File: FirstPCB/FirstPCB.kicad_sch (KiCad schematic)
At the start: 5 parts, among them U1 STM32G0B1KETx

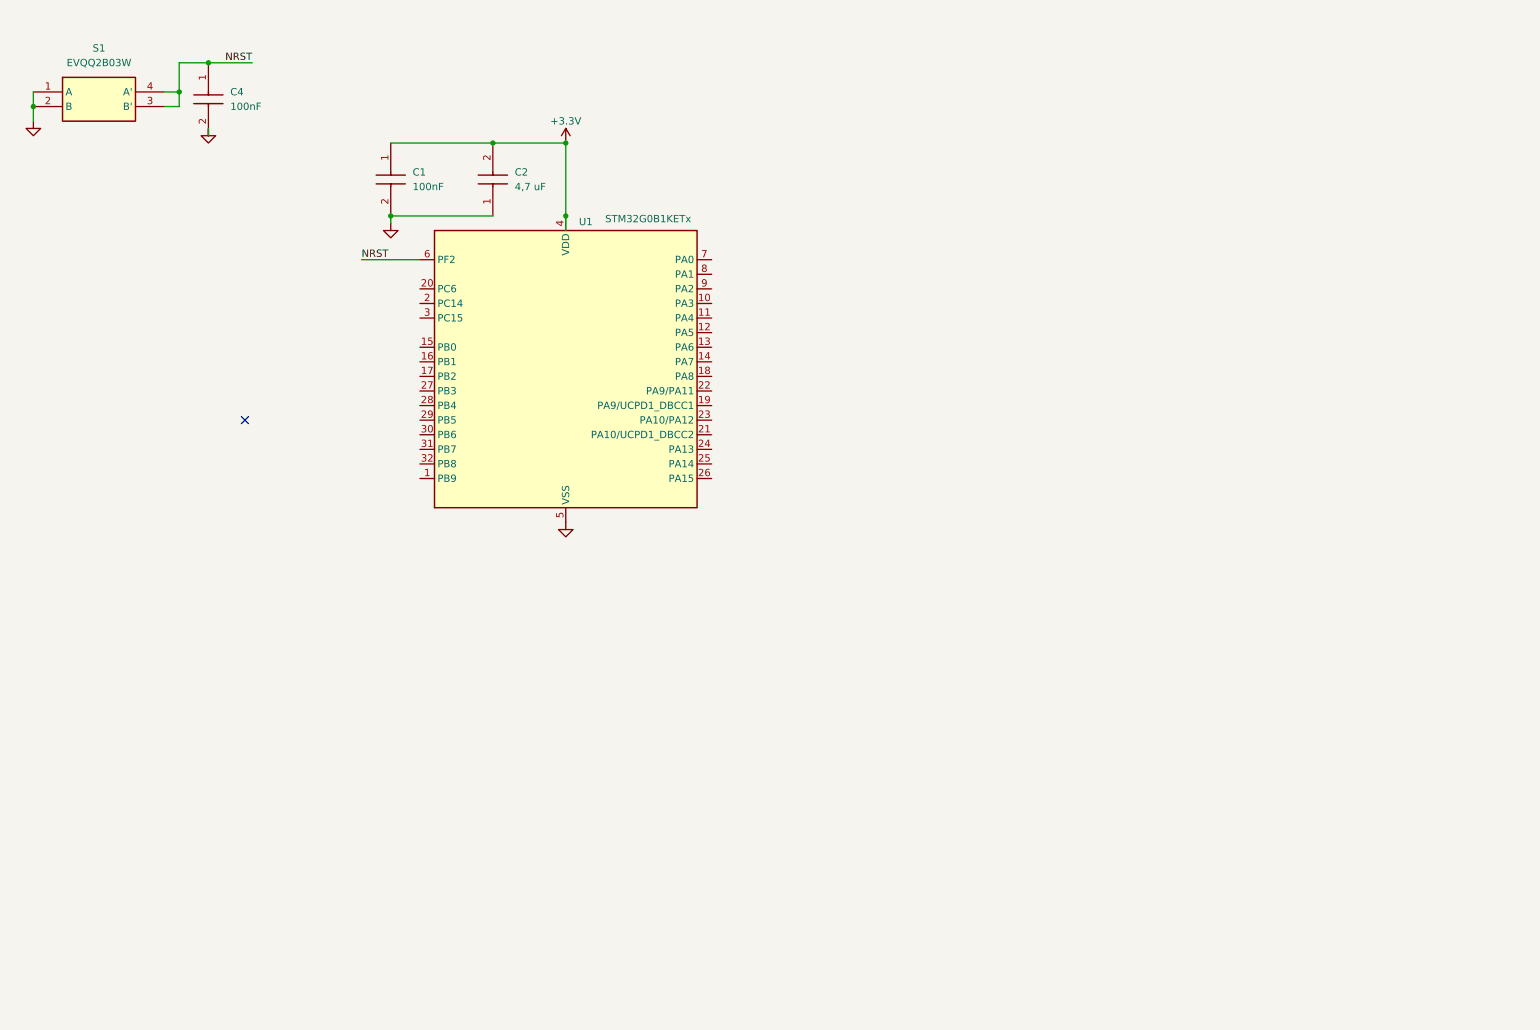
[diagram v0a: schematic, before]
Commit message: added Voltage Regulator
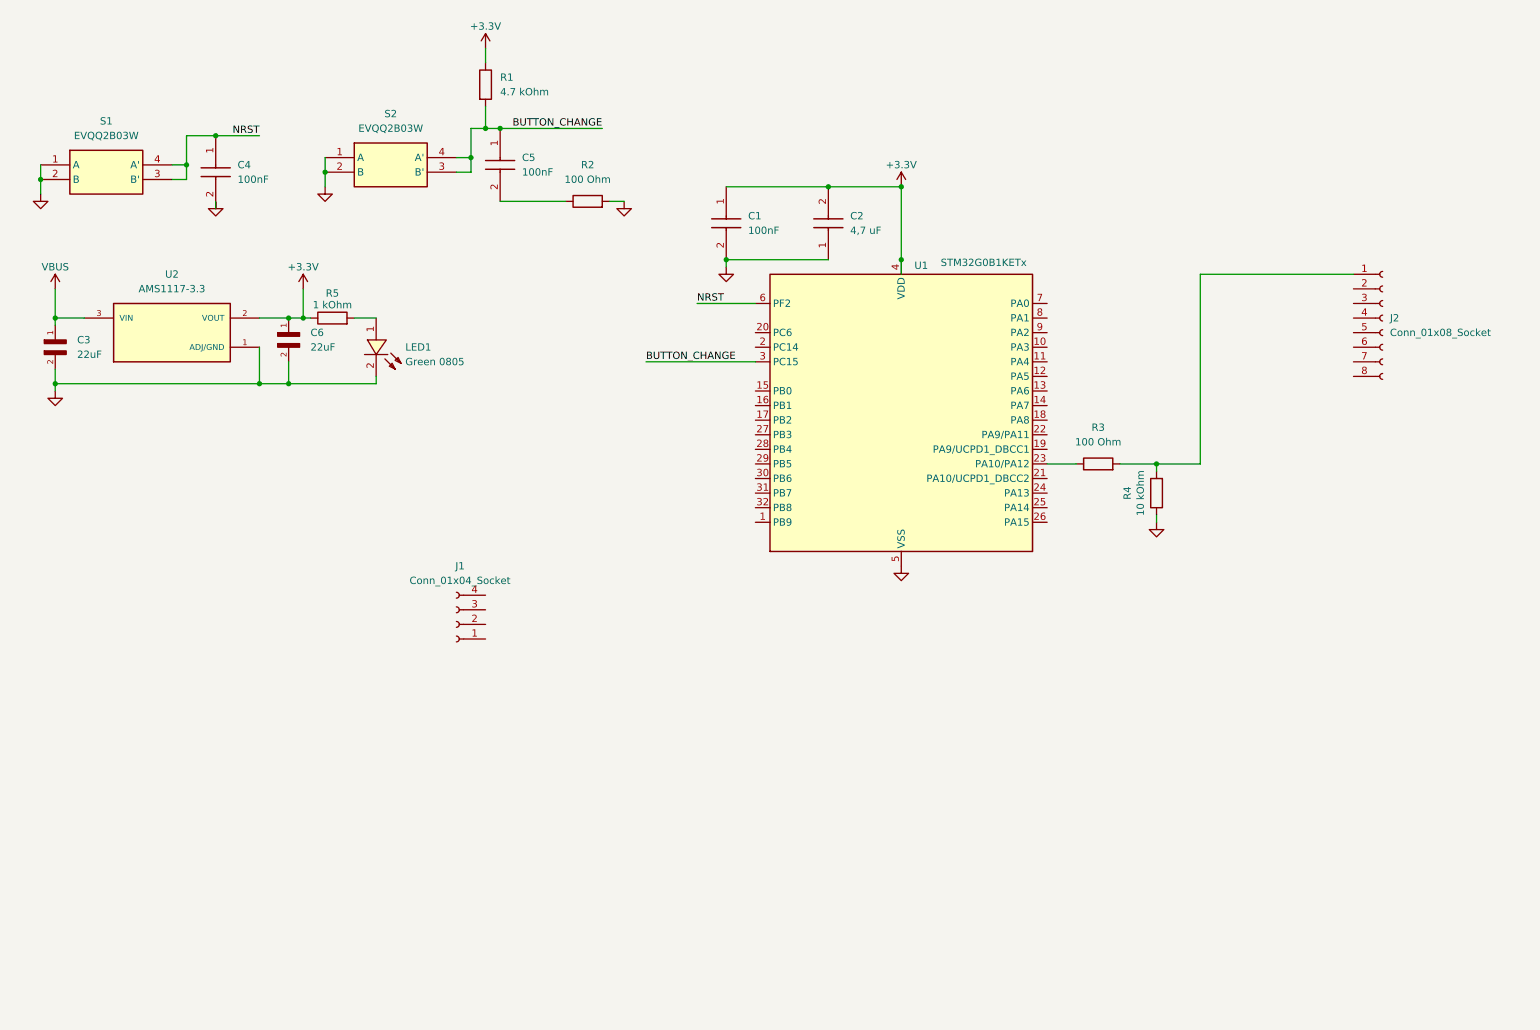
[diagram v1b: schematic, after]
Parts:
- added C3, C6: 22uF, CL21A226MQQNNNE:CAPC2012X140N, symbol CL21A226MQQNNNE:CL21A226MQQNNNE
- added C5: 100nF, SamacSys_Parts:CAPC2012X95N, symbol SamacSys_Parts:CL21B104KBCNNNC
- added J1: Conn_01x04_Socket, Connector_PinSocket_2.54mm:PinSocket_1x04_P2.54mm_Vertical, symbol Connector:Conn_01x04_Socket
- added J2: Conn_01x08_Socket, Connector_PinSocket_2.54mm:PinSocket_1x08_P2.54mm_Vertical, symbol Connector:Conn_01x08_Socket
- added LED1: Green 0805, C2292:LED0805-R-RD, symbol Yellow_green_0805:Yellowgreen0805
- added R1: 4.7 kOhm, Resistor_SMD:R_0805_2012Metric, symbol Device:R
- added R2, R3: 100 Ohm, Resistor_SMD:R_0805_2012Metric, symbol Device:R
- added R4: 10 kOhm, Resistor_SMD:R_0805_2012Metric, symbol Device:R
- added R5: 1 kOhm, Resistor_SMD:R_0805_2012Metric, symbol Device:R
- added S2: EVQQ2B03W, SamacSys_Parts:EVQQ2, symbol SamacSys_Parts:EVQQ2B03W
- added U2: AMS1117-3.3, AMS1117-3.3:SOT229P700X180-4N, symbol AMS1117-3.3:AMS1117-3.3
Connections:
- net +3.3V: now also C6.1, R1.1, R5.1, U2.2 (VOUT)
- net GND: now also C3.2, C6.2, LED1.2, R2.2, R4.1, S2.1 (A), S2.2 (B), U2.1 (ADJ/GND)
- net at U1.23 (PA10/PA12): now also R3.1
- net BUTTON_CHANGE: now reaches U1.3 (PC15)
- net BUTTON_CHANGE: now also C5.1, R1.2, S2.3 (B'), S2.4 (A')
- new net: J2.1 (Pin_1), R3.2, R4.2
- new net: C5.2, R2.1
- new net: LED1.1, R5.2
- new net VBUS: C3.1, U2.3 (VIN)
- no-connect marks 1 -> 0
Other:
- moved on the sheet: C1, C2, C4, S1, U1

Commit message: added sensor and schematic update
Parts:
- added IC1: ENS210-LQFM, SON95P200X200X80-5N, symbol SamacSys_Parts:ENS210-LQFM
- added J3, J4, J5: Conn_01x04_Socket, Connector_PinSocket_2.54mm:PinSocket_1x04_P2.54mm_Vertical, symbol Connector:Conn_01x04_Socket
- added R6, R7: 4.7 kOhm, Resistor_SMD:R_0805_2012Metric, symbol Device:R
- renumbered J2 to J1, J1 to J2
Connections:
- net +3.3V: now also J1.8 (Pin_8), IC1.1 (VDD), J3.1 (Pin_1), R6.1, R7.1
- net GND: now also J1.7 (Pin_7), IC1.4 (VSS_1), IC1.5 (VSS_2), J3.4 (Pin_4)
- net UART_RX: now reaches U1.10 (PA3)
- net UART_RX: now also J5.3 (Pin_3)
- net ADC_IN_4: now reaches U1.11 (PA4)
- net ADC_IN_4: now also J5.2 (Pin_2)
- net ADC_IN_5: now reaches U1.12 (PA5)
- net ADC_IN_5: now also J5.1 (Pin_1)
- net SENSOR_SDA: now reaches U1.13 (PA6)
- net SENSOR_SDA: now also IC1.3 (SDA), R7.2
- net SENSOR_SCL: now reaches U1.14 (PA7)
- net SENSOR_SCL: now also IC1.2 (SCL), R6.2
- net DISP_LED: now reaches U1.20 (PC6)
- net DISP_LED: now also R3.1
- net DISP_RES: now reaches U1.21 (PA10/UCPD1_DBCC2)
- net DISP_RES: now also J1.5 (Pin_5)
- net DISP_DC: now reaches U1.22 (PA9/PA11)
- net DISP_DC: now also J1.4 (Pin_4)
- net at U1.23 (PA10/PA12): no longer R3.1
- net SW_DIO: now reaches U1.24 (PA13)
- net SW_DIO: now also J3.2 (Pin_2)
- net SW_CLK: now reaches U1.25 (PA14)
- net SW_CLK: now also J3.3 (Pin_3)
- net DISP_CS: now reaches U1.26 (PA15)
- net DISP_CS: now also J1.6 (Pin_6)
- net DISP_MISO: now reaches U1.27 (PB3)
- net SD_CS: now reaches U1.28 (PB4)
- net SD_CS: now also J2.4 (Pin_4), J4.4 (Pin_4)
- net DISP_MOSI: now reaches U1.29 (PB5)
- net DISP_MOSI: now also J1.3 (Pin_3)
- net SD_MISO: now reaches U1.30 (PB6)
- net SD_MISO: now also J2.2 (Pin_2), J4.2 (Pin_2)
- net SD_MOSI: now reaches U1.31 (PB7)
- net SD_MOSI: now also J2.3 (Pin_3), J4.3 (Pin_3)
- net SD_SCK: now reaches U1.32 (PB8)
- net SD_SCK: now also J2.1 (Pin_1), J4.1 (Pin_1)
- net UART_TX: now reaches U1.9 (PA2)
- net UART_TX: now also J5.4 (Pin_4)
- net DISP_SCK: now reaches J1.2 (Pin_2)
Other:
- title: STM32->Display -> First PCB
- moved on the sheet: C1, C2, C5, J1, J2, R1, R2, R3, R4, S2, U1

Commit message: shematic finished
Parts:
- removed J4: Conn_01x04_Socket, Connector_PinSocket_2.54mm:PinSocket_1x04_P2.54mm_Vertical, symbol Connector:Conn_01x04_Socket
- added R8, R9: 5.1 kOhm, Resistor_SMD:R_0805_2012Metric, symbol Device:R
- added USB1: TYPE-C_6P, Connector_USB:USB_C_Receptacle_GCT_USB4135-GF-A_6P_TopMnt_Horizontal, symbol JLCImport:TYPE-C_6P
- IC1: footprint SON95P200X200X80-5N -> SamacSys_Parts:SON95P200X200X80-5N
- LED1: footprint C2292:LED0805-R-RD -> CRG1206F470R:RESC3115X65N
- U2: footprint AMS1117-3.3:SOT229P700X180-4N -> Package_TO_SOT_SMD:SOT-223-3_TabPin2
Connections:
- net GND: now also R8.1, R9.1, USB1.A12 (GND), USB1.B12 (GND), USB1.SH
- net VBUS: now also USB1.A9 (VBUS), USB1.B9 (VBUS)
- new net: R9.2, USB1.B5 (CC2)
- new net: R8.2, USB1.A5 (CC1)
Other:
- note added: "Button CHANGE"
- note added: "CPU"
- note added: "Connectors Female"
- note added: "DISPLAY"
- note added: "NRESET"
- note added: "Power"
- note added: "SD CARD"
- note added: "SWD & Programming"
- note added: "Temperature & Humidity Sensor"
- note added: "UART & ADC"
- company: (none) -> Smart Avtomatic & Granitovich
- moved on the sheet: C1, C2, C3, C4, C5, C6, IC1, J1, J2, J3, J5, LED1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

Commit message: before routing
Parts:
- renumbered J5 to J4
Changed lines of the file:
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@@
 		(in_pos_files yes)
 		(dnp no)
-		(property "Reference" "J5"
+		(property "Reference" "J4"
 			(at 258.826 110.998 0)
 			(show_name no)
@@
 			(project "FirstPCB"
 				(path "/8332f25c-6806-4968-af8e-1051e6f60ffc"
-					(reference "J5")
+					(reference "J4")
 					(unit 1)
 				)

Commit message: update gerber
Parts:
- J1, J2, J3, J4: now left out of the parts list
- LED1: MANUFACTURER (none) -> KENTO; Manufacturer KENTO -> (none)
- U2: PACKAGE SOT-223 ams -> (none); PRICE None -> (none)
- USB1: MANUFACTURER (none) -> SHOU HAN; Manufacturer SHOU HAN -> (none)
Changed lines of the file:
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@@
 		(body_style 1)
 		(exclude_from_sim no)
-		(in_bom yes)
+		(in_bom no)
 		(on_board yes)
 		(in_pos_files yes)
@@
 		(body_style 1)
 		(exclude_from_sim no)
-		(in_bom yes)
+		(in_bom no)
 		(on_board yes)
 		(in_pos_files yes)
@@
 			)
 		)
-		(property "PACKAGE" "SOT-223 ams"
+		(property "Package" "SOT-223 ams"
 			(at 99.06 39.37 0)
 			(hide yes)
@@
 			)
 		)
-		(property "PRICE" "None"
+		(property "Price" "None"
 			(at 99.06 39.37 0)
 			(hide yes)
@@
 		(body_style 1)
 		(exclude_from_sim no)
-		(in_bom yes)
+		(in_bom no)
 		(on_board yes)
 		(in_pos_files yes)
@@
 			)
 		)
-		(property "Manufacturer" "KENTO"
+		(property "MANUFACTURER" "KENTO"
 			(at 121.92 41.91 0)
 			(hide yes)
@@
 		(body_style 1)
 		(exclude_from_sim no)
-		(in_bom yes)
+		(in_bom no)
 		(on_board yes)
 		(in_pos_files yes)
@@
 			)
 		)
-		(property "Manufacturer" "SHOU HAN"
+		(property "MANUFACTURER" "SHOU HAN"
 			(at 53.34 39.37 0)
 			(hide yes)

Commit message: design finished, ordered pcb
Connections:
- net DISP_MISO is gone; now on net DISP_SCK: U1.27 (PB3)
- net +3.3V: now also J3.3 (Pin_3); no longer J3.1 (Pin_1)
- net DISP_LED: now also U1.8 (PA1); no longer U1.20 (PC6)
- net SD_CS: now also J2.1 (Pin_1); no longer J2.4 (Pin_4)
- net SD_MISO: now also J2.3 (Pin_3); no longer J2.2 (Pin_2)
- net SD_MOSI: now also J2.2 (Pin_2); no longer J2.3 (Pin_3)
- net SD_SCK: now also J2.4 (Pin_4); no longer J2.1 (Pin_1)
- net SW_CLK: now also J3.2 (Pin_2); no longer J3.3 (Pin_3)
- net SW_DIO: now also J3.1 (Pin_1); no longer J3.2 (Pin_2)
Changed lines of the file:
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@@
 	(wire
 		(pts
-			(xy 46.99 173.99) (xy 46.99 176.53)
+			(xy 241.3 46.99) (xy 251.46 46.99)
 		)
 		(stroke
@@
 	(wire
 		(pts
-			(xy 241.3 49.53) (xy 251.46 49.53)
+			(xy 46.99 173.99) (xy 46.99 176.53)
 		)
 		(stroke
@@
 	(wire
 		(pts
-			(xy 128.27 99.06) (xy 139.7 99.06)
+			(xy 73.66 88.9) (xy 73.66 83.82)
 		)
 		(stroke
@@
 	(wire
 		(pts
-			(xy 73.66 88.9) (xy 73.66 83.82)
+			(xy 78.74 36.83) (xy 78.74 31.75)
 		)
 		(stroke
@@
 	(wire
 		(pts
-			(xy 78.74 36.83) (xy 78.74 31.75)
+			(xy 114.3 41.91) (xy 114.3 48.26)
 		)
 		(stroke
@@
 	(wire
 		(pts
-			(xy 114.3 41.91) (xy 114.3 48.26)
+			(xy 21.59 179.07) (xy 21.59 176.53)
 		)
 		(stroke
@@
 	(wire
 		(pts
-			(xy 21.59 179.07) (xy 21.59 176.53)
+			(xy 201.93 96.52) (xy 190.5 96.52)
 		)
 		(stroke
@@
 	(wire
 		(pts
-			(xy 242.57 46.99) (xy 242.57 45.72)
+			(xy 238.76 45.72) (xy 238.76 52.07)
 		)
 		(stroke
@@
 	(wire
 		(pts
+			(xy 241.3 49.53) (xy 251.46 49.53)
+		)
+		(stroke
+			(width 0)
+			(type default)
+		)
+	)
+	(wire
+		(pts
 			(xy 19.05 46.99) (xy 19.05 48.26)
 		)
@@
 	(wire
 		(pts
-			(xy 251.46 46.99) (xy 242.57 46.99)
-		)
-		(stroke
-			(width 0)
-			(type default)
-		)
-	)
-	(wire
-		(pts
 			(xy 121.92 36.83) (xy 123.19 36.83)
 		)
@@
 	(wire
 		(pts
-			(xy 241.3 52.07) (xy 251.46 52.07)
-		)
-		(stroke
-			(width 0)
-			(type default)
-		)
-	)
-	(wire
-		(pts
 			(xy 35.56 74.93) (xy 35.56 76.2)
 		)
@@
 	(wire
 		(pts
-			(xy 242.57 54.61) (xy 251.46 54.61)
+			(xy 238.76 54.61) (xy 251.46 54.61)
+		)
+		(stroke
+			(width 0)
+			(type default)
+		)
+	)
+	(wire
+		(pts
+			(xy 238.76 52.07) (xy 251.46 52.07)
 		)
 		(stroke
@@
 		)
 	)
-	(label "DISP_MISO"
+	(label "DISP_SCK"
 		(at 129.54 116.84 0)
 		(effects
@@
 		)
 	)
-	(label "SD_CS"
+	(label "SD_SCK"
 		(at 241.3 82.55 0)
 		(effects
@@
 		)
 	)
+	(label "SW_DIO"
+		(at 241.3 46.99 0)
+		(effects
+			(font
+				(size 1.27 1.27)
+			)
+			(justify left bottom)
+		)
+	)
 	(label "DISP_RES"
 		(at 247.65 144.78 0)
@@
 	)
 	(label "SW_CLK"
+		(at 241.3 49.53 0)
+		(effects
+			(font
+				(size 1.27 1.27)
+			)
+			(justify left bottom)
+		)
+	)
+	(label "SW_CLK"
 		(at 200.66 129.54 180)
 		(effects
@@
 		)
 	)
-	(label "SD_MOSI"
+	(label "SD_MISO"
 		(at 241.3 80.01 0)
 		(effects
@@
 		)
 	)
-	(label "SD_SCK"
+	(label "SD_CS"
 		(at 241.3 74.93 0)
 		(effects
@@
 		)
 	)
-	(label "SW_DIO"
-		(at 241.3 49.53 0)
+	(label "DISP_LED"
+		(at 201.93 96.52 180)
 		(effects
 			(font
 				(size 1.27 1.27)
 			)
-			(justify left bottom)
+			(justify right bottom)
 		)
 	)
@@
 		)
 	)
-	(label "DISP_LED"
-		(at 128.27 99.06 0)
-		(effects
-			(font
-				(size 1.27 1.27)
-			)
-			(justify left bottom)
-		)
-	)
-	(label "SD_MISO"
+	(label "SD_MOSI"
 		(at 241.3 77.47 0)
 		(effects
@@
 		)
 	)
-	(label "SW_CLK"
-		(at 241.3 52.07 0)
-		(effects
-			(font
-				(size 1.27 1.27)
-			)
-			(justify left bottom)
-		)
-	)
 	(label "SENSOR_SDA"
 		(at 99.06 86.36 180)
@@
 	(symbol
 		(lib_id "power:GND")
-		(at 242.57 54.61 0)
+		(at 238.76 54.61 0)
 		(unit 1)
 		(body_style 1)
@@
 		(fields_autoplaced yes)
 		(property "Reference" "#PWR018"
-			(at 242.57 60.96 0)
+			(at 238.76 60.96 0)
 			(hide yes)
 			(show_name no)
@@
 		)
 		(property "Value" "GND"
-			(at 242.57 59.69 0)
+			(at 238.76 59.69 0)
 			(hide yes)
 			(show_name no)
@@
 		)
 		(property "Footprint" ""
-			(at 242.57 54.61 0)
+			(at 238.76 54.61 0)
 			(hide yes)
 			(show_name no)
@@
 		)
 		(property "Datasheet" ""
-			(at 242.57 54.61 0)
+			(at 238.76 54.61 0)
 			(hide yes)
 			(show_name no)
@@
 		)
 		(property "Description" ""
-			(at 242.57 54.61 0)
+			(at 238.76 54.61 0)
 			(hide yes)
 			(show_name no)
@@
 			)
 		)
-		(property "Package" "SOT-223 ams"
-			(at 99.06 39.37 0)
-			(hide yes)
-			(show_name no)
-			(do_not_autoplace no)
-			(effects
-				(font
-					(size 1.27 1.27)
-				)
-				(justify bottom)
-			)
-		)
-		(property "Price" "None"
-			(at 99.06 39.37 0)
-			(hide yes)
-			(show_name no)
-			(do_not_autoplace no)
-			(effects
-				(font
-					(size 1.27 1.27)
-				)
-				(justify bottom)
-			)
-		)
 		(property "Package" "SOT-223-3L UMW"
 			(at 99.06 39.37 0)
@@
 	(symbol
 		(lib_id "power:+3.3V")
-		(at 242.57 45.72 0)
+		(at 238.76 45.72 0)
 		(unit 1)
 		(body_style 1)
@@
 		(dnp no)
 		(property "Reference" "#PWR017"
-			(at 242.57 49.53 0)
+			(at 238.76 49.53 0)
 			(hide yes)
 			(show_name no)
@@
 		)
 		(property "Value" "+3.3V"
-			(at 239.014 45.72 0)
+			(at 234.696 45.466 0)
 			(show_name no)
 			(do_not_autoplace no)
@@
 		)
 		(property "Footprint" ""
-			(at 242.57 45.72 0)
+			(at 238.76 45.72 0)
 			(hide yes)
 			(show_name no)
@@
 		)
 		(property "Datasheet" ""
-			(at 242.57 45.72 0)
+			(at 238.76 45.72 0)
 			(hide yes)
 			(show_name no)
@@
 		)
 		(property "Description" ""
-			(at 242.57 45.72 0)
+			(at 238.76 45.72 0)
 			(hide yes)
 			(show_name no)

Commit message: Fix Resistor
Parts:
- R5: value 1 kOhm -> 100 Ohm
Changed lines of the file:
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@@
 	)
 	(junction
-		(at 121.92 36.83)
-		(diameter 0)
-		(color 0 0 0 0)
-	)
-	(junction
 		(at 165.1 73.66)
 		(diameter 0)
@@
 	(wire
 		(pts
-			(xy 121.92 36.83) (xy 123.19 36.83)
-		)
-		(stroke
-			(width 0)
-			(type default)
-		)
-	)
-	(wire
-		(pts
 			(xy 134.62 48.26) (xy 119.38 48.26)
 		)
@@
 	(wire
 		(pts
-			(xy 121.92 31.75) (xy 121.92 36.83)
+			(xy 119.38 31.75) (xy 119.38 36.83)
 		)
 		(stroke
@@
 	(wire
 		(pts
-			(xy 119.38 36.83) (xy 121.92 36.83)
+			(xy 68.58 39.37) (xy 68.58 41.91)
 		)
 		(stroke
@@
 	(wire
 		(pts
-			(xy 68.58 39.37) (xy 68.58 41.91)
+			(xy 119.38 36.83) (xy 123.19 36.83)
 		)
 		(stroke
@@
 	(symbol
 		(lib_id "power:+3.3V")
-		(at 121.92 31.75 0)
+		(at 119.38 31.75 0)
 		(unit 1)
 		(body_style 1)
@@
 		(dnp no)
 		(property "Reference" "#PWR07"
-			(at 121.92 35.56 0)
+			(at 119.38 35.56 0)
 			(hide yes)
 			(show_name no)
@@
 		)
 		(property "Value" "+3.3V"
-			(at 124.206 27.686 0)
+			(at 121.666 27.686 0)
 			(show_name no)
 			(do_not_autoplace no)
@@
 		)
 		(property "Footprint" ""
-			(at 121.92 31.75 0)
+			(at 119.38 31.75 0)
 			(hide yes)
 			(show_name no)
@@
 		)
 		(property "Datasheet" ""
-			(at 121.92 31.75 0)
+			(at 119.38 31.75 0)
 			(hide yes)
 			(show_name no)
@@
 		)
 		(property "Description" ""
-			(at 121.92 31.75 0)
+			(at 119.38 31.75 0)
 			(hide yes)
 			(show_name no)
@@
 			)
 		)
-		(property "Value" "1 kOhm"
+		(property "Value" "100 Ohm"
 			(at 127 34.544 90)
 			(show_name no)
